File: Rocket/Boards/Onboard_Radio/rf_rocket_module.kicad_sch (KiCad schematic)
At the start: 12 parts

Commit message: schematic ready for review
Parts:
- R17, R18, R19: MPN (none) -> CRCW06030000Z0EA; Manufacturer (none) -> Vishay Dale
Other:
- sheet CAN_Termination ports: added none; removed CAN2_RX, CAN2_TX, CAN_STB2
- sheet MCU ports: added none; removed CAN2_RX, CAN2_TX, CAN_STB2
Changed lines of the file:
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@@
+	(wire
+		(pts
+			(xy 53.34 105.41) (xy 77.47 105.41)
+		)
+		(stroke
+			(width 0)
+			(type default)
+		)
+	)
 	(wire
 		(pts
@@
 	(wire
 		(pts
-			(xy 53.34 87.63) (xy 77.47 87.63)
-		)
-		(stroke
-			(width 0)
-			(type default)
-		)
-	)
-	(wire
-		(pts
 			(xy 124.46 22.86) (xy 157.48 22.86)
 		)
@@
 	(wire
 		(pts
-			(xy 53.34 97.79) (xy 77.47 97.79)
-		)
-		(stroke
-			(width 0)
-			(type default)
-		)
-	)
-	(wire
-		(pts
 			(xy 43.18 166.37) (xy 49.53 166.37)
 		)
@@
 	(wire
 		(pts
-			(xy 53.34 90.17) (xy 77.47 90.17)
-		)
-		(stroke
-			(width 0)
-			(type default)
-		)
-	)
-	(wire
-		(pts
 			(xy 54.61 22.86) (xy 52.07 22.86)
 		)
@@
 		(pts
 			(xy 43.18 173.99) (xy 49.53 173.99)
-		)
-		(stroke
-			(width 0)
-			(type default)
-		)
-	)
-	(wire
-		(pts
-			(xy 53.34 105.41) (xy 77.47 105.41)
 		)
 		(stroke
@@
 			)
 		)
-		(property "Datasheet" ""
+		(property "Datasheet" "https://www.vishay.com/docs/20035/dcrcwe3.pdf"
 			(at 58.42 33.02 0)
 			(hide yes)
@@
 			)
 		)
-		(property "Description" "Resistor"
+		(property "Description" "0 Ohms Jumper 0.125W, 1/8W Chip Resistor 0603 (1608 Metric) Automotive AEC-Q200 Thick Film"
 			(at 58.42 33.02 0)
 			(hide yes)
@@
 		)
 		(property "KLC_S4.1" ""
+			(at 58.42 33.02 90)
+			(hide yes)
+			(show_name no)
+			(do_not_autoplace no)
+			(effects
+				(font
+					(size 1.27 1.27)
+				)
+			)
+		)
+		(property "MPN" "CRCW06030000Z0EA"
+			(at 58.42 33.02 90)
+			(hide yes)
+			(show_name no)
+			(do_not_autoplace no)
+			(effects
+				(font
+					(size 1.27 1.27)
+				)
+			)
+		)
+		(property "Manufacturer" "Vishay Dale"
 			(at 58.42 33.02 90)
 			(hide yes)
@@
 			)
 		)
-		(property "Datasheet" ""
+		(property "Datasheet" "https://www.vishay.com/docs/20035/dcrcwe3.pdf"
 			(at 58.42 27.94 0)
 			(hide yes)
@@
 			)
 		)
-		(property "Description" "Resistor"
+		(property "Description" "0 Ohms Jumper 0.125W, 1/8W Chip Resistor 0603 (1608 Metric) Automotive AEC-Q200 Thick Film"
 			(at 58.42 27.94 0)
 			(hide yes)
@@
 		)
 		(property "KLC_S4.1" ""
+			(at 58.42 27.94 90)
+			(hide yes)
+			(show_name no)
+			(do_not_autoplace no)
+			(effects
+				(font
+					(size 1.27 1.27)
+				)
+			)
+		)
+		(property "MPN" "CRCW06030000Z0EA"
+			(at 58.42 27.94 90)
+			(hide yes)
+			(show_name no)
+			(do_not_autoplace no)
+			(effects
+				(font
+					(size 1.27 1.27)
+				)
+			)
+		)
+		(property "Manufacturer" "Vishay Dale"
 			(at 58.42 27.94 90)
 			(hide yes)
@@
 			)
 		)
-		(property "Datasheet" ""
+		(property "Datasheet" "https://www.vishay.com/docs/20035/dcrcwe3.pdf"
 			(at 58.42 22.86 0)
 			(hide yes)
@@
 			)
 		)
-		(property "Description" "Resistor"
+		(property "Description" "0 Ohms Jumper 0.125W, 1/8W Chip Resistor 0603 (1608 Metric) Automotive AEC-Q200 Thick Film"
 			(at 58.42 22.86 0)
 			(hide yes)
@@
 		)
 		(property "KLC_S4.1" ""
+			(at 58.42 22.86 90)
+			(hide yes)
+			(show_name no)
+			(do_not_autoplace no)
+			(effects
+				(font
+					(size 1.27 1.27)
+				)
+			)
+		)
+		(property "MPN" "CRCW06030000Z0EA"
+			(at 58.42 22.86 90)
+			(hide yes)
+			(show_name no)
+			(do_not_autoplace no)
+			(effects
+				(font
+					(size 1.27 1.27)
+				)
+			)
+		)
+		(property "Manufacturer" "Vishay Dale"
 			(at 58.42 22.86 90)
 			(hide yes)
@@
 			)
 		)
+		(pin "CAN1_RX" input
+			(at 77.47 80.01 180)
+			(effects
+				(font
+					(size 1.27 1.27)
+				)
+				(justify left)
+			)
+		)
+		(pin "CAN1_TX" input
+			(at 77.47 82.55 180)
+			(effects
+				(font
+					(size 1.27 1.27)
+				)
+				(justify left)
+			)
+		)
+		(pin "CAN_STB1" input
+			(at 77.47 95.25 180)
+			(effects
+				(font
+					(size 1.27 1.27)
+				)
+				(justify left)
+			)
+		)
 		(pin "CAN2_AUX" input
 			(at 77.47 105.41 180)
-			(effects
-				(font
-					(size 1.27 1.27)
-				)
-				(justify left)
-			)
-		)
-		(pin "CAN1_RX" input
-			(at 77.47 80.01 180)
-			(effects
-				(font
-					(size 1.27 1.27)
-				)
-				(justify left)
-			)
-		)
-		(pin "CAN1_TX" input
-			(at 77.47 82.55 180)
-			(effects
-				(font
-					(size 1.27 1.27)
-				)
-				(justify left)
-			)
-		)
-		(pin "CAN2_RX" input
-			(at 77.47 87.63 180)
-			(effects
-				(font
-					(size 1.27 1.27)
-				)
-				(justify left)
-			)
-		)
-		(pin "CAN2_TX" input
-			(at 77.47 90.17 180)
-			(effects
-				(font
-					(size 1.27 1.27)
-				)
-				(justify left)
-			)
-		)
-		(pin "CAN_STB1" input
-			(at 77.47 95.25 180)
-			(effects
-				(font
-					(size 1.27 1.27)
-				)
-				(justify left)
-			)
-		)
-		(pin "CAN_STB2" input
-			(at 77.47 97.79 180)
 			(effects
 				(font
@@
 			)
 		)
+		(pin "CAN_PWR_IN" input
+			(at 53.34 74.93 0)
+			(effects
+				(font
+					(size 1.27 1.27)
+				)
+				(justify right)
+			)
+		)
+		(pin "CAN_STB1" input
+			(at 53.34 95.25 0)
+			(effects
+				(font
+					(size 1.27 1.27)
+				)
+				(justify right)
+			)
+		)
 		(pin "CAN2_AUX" input
 			(at 53.34 105.41 0)
 			(effects
 				(font
-					(size 1.27 1.27)
-				)
-				(justify right)
-			)
-		)
-		(pin "CAN_PWR_IN" input
-			(at 53.34 74.93 0)
-			(effects
-				(font
-					(size 1.27 1.27)
-				)
-				(justify right)
-			)
-		)
-		(pin "CAN2_RX" input
-			(at 53.34 90.17 0)
-			(effects
-				(font
-					(size 1.27 1.27)
-				)
-				(justify right)
-			)
-		)
-		(pin "CAN2_TX" input
-			(at 53.34 87.63 0)
-			(effects
-				(font
-					(size 1.27 1.27)
-				)
-				(justify right)
-			)
-		)
-		(pin "CAN_STB1" input
-			(at 53.34 95.25 0)
-			(effects
-				(font
-					(size 1.27 1.27)
-				)
-				(justify right)
-			)
-		)
-		(pin "CAN_STB2" input
-			(at 53.34 97.79 0)
-			(effects
-				(font

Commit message: updates
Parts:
- removed R17, R18, R19: 0R, Resistor_SMD:R_0603_1608Metric, symbol Device:R
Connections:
- net Power Input/+7V4 renamed Power Input/+7V4_Input
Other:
- sheet Power Input ports: added +3V3A_Input, +3V3_Input, +5V_Input, +7V4_Input; removed +3V3, +3V3A, +5V, +7V4
- moved on the sheet: R20

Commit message: everything minus trace impedance and via stictching
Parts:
- H1, H2, H3, H4: footprint MountingHole:MountingHole_3.2mm_M3 -> MountingHole:MountingHole_3.2mm_M3_DIN965_Pad
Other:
- sheet MCU ports: added 3V3A_LDO_EN, 3V3_LDO_EN; removed none
- sheet Power Input ports: added 3V3A_LDO_EN, 3V3_LDO_EN; removed none
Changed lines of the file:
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@@
+	(wire
+		(pts
+			(xy 52.07 46.99) (xy 77.47 46.99)
+		)
+		(stroke
+			(width 0)
+			(type default)
+		)
+	)
 	(wire
 		(pts
@@
 		(pts
 			(xy 153.67 44.45) (xy 157.48 44.45)
+		)
+		(stroke
+			(width 0)
+			(type default)
+		)
+	)
+	(wire
+		(pts
+			(xy 52.07 49.53) (xy 77.47 49.53)
 		)
 		(stroke
@@
 			)
 		)
-		(property "Footprint" "MountingHole:MountingHole_3.2mm_M3"
+		(property "Footprint" "MountingHole:MountingHole_3.2mm_M3_DIN965_Pad"
 			(at 40.64 166.37 0)
 			(hide yes)
@@
 			)
 		)
-		(property "Footprint" "MountingHole:MountingHole_3.2mm_M3"
+		(property "Footprint" "MountingHole:MountingHole_3.2mm_M3_DIN965_Pad"
 			(at 40.64 151.13 0)
 			(hide yes)
@@
 			)
 		)
-		(property "Footprint" "MountingHole:MountingHole_3.2mm_M3"
+		(property "Footprint" "MountingHole:MountingHole_3.2mm_M3_DIN965_Pad"
 			(at 40.64 173.99 0)
 			(hide yes)
@@
 			)
 		)
-		(property "Footprint" "MountingHole:MountingHole_3.2mm_M3"
+		(property "Footprint" "MountingHole:MountingHole_3.2mm_M3_DIN965_Pad"
 			(at 40.64 158.75 0)
 			(hide yes)
@@
 			)
 		)
+		(pin "3V3A_LDO_EN" input
+			(at 52.07 46.99 0)
+			(effects
+				(font
+					(size 1.27 1.27)
+				)
+				(justify right)
+			)
+		)
+		(pin "3V3_LDO_EN" input
+			(at 52.07 49.53 0)
+			(effects
+				(font
+					(size 1.27 1.27)
+				)
+				(justify right)
+			)
+		)
 		(instances
 			(project "rf_rocket_module"
@@
 			(effects
 				(font
+					(size 1.27 1.27)
+				)
+				(justify left)
+			)
+		)
+		(pin "3V3A_LDO_EN" input
+			(at 77.47 46.99 180)
+			(effects
+				(font
+					(size 1.27 1.27)
+				)
+				(justify left)
+			)
+		)
+		(pin "3V3_LDO_EN" input
+			(at 77.47 49.53 180)
+			(effects
+				(font

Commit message: needs pcb and schematic review
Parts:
- R20: LCSC Part # (none) -> C844915
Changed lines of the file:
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@@
+			)
+		)
+		(property "LCSC Part #" "C844915"
+			(at 58.42 38.1 90)
+			(hide yes)
+			(show_name no)
+			(do_not_autoplace no)
+			(effects
+				(font
+					(size 1.27 1.27)
+				)
 			)
 		)

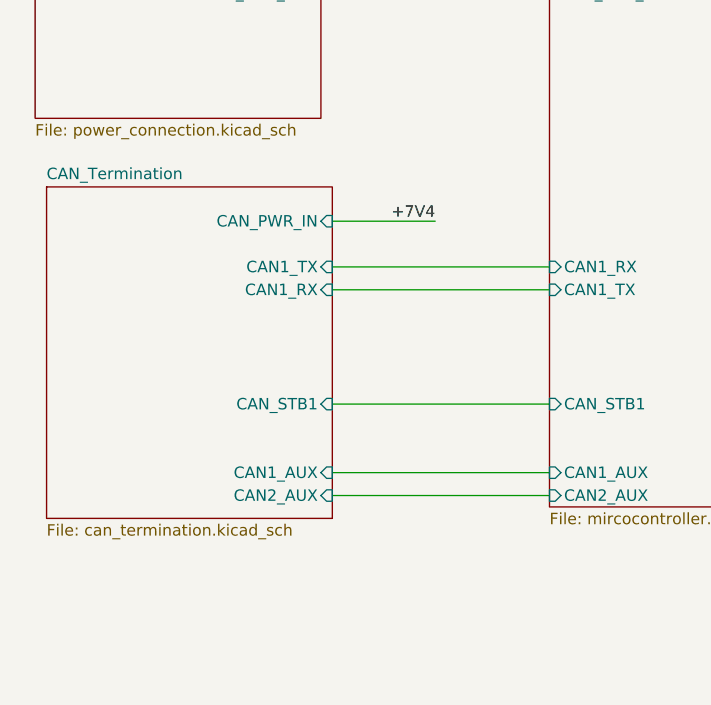
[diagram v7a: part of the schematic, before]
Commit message: updated swd and crystal
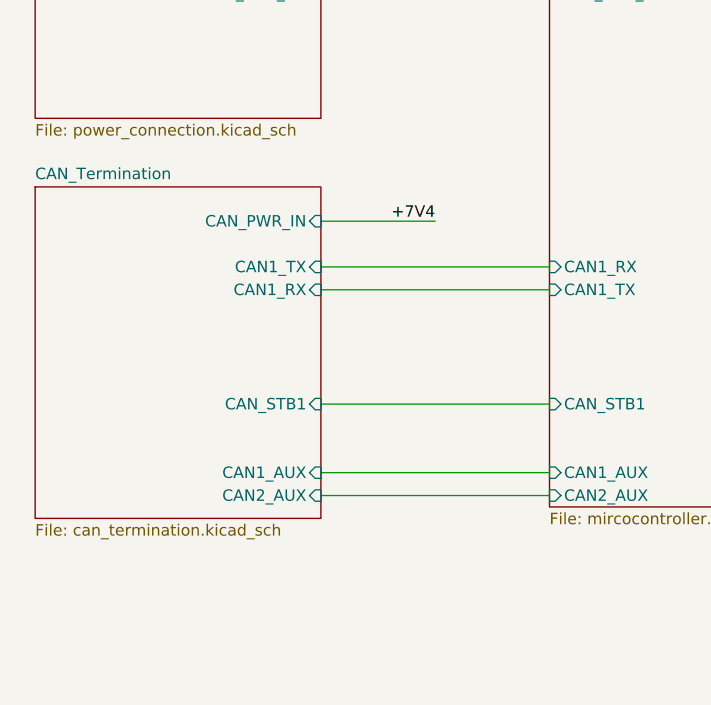
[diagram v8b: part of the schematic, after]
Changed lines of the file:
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@@
 	(wire
 		(pts
-			(xy 53.34 105.41) (xy 77.47 105.41)
+			(xy 52.07 105.41) (xy 77.47 105.41)
 		)
 		(stroke
@@
 	(wire
 		(pts
-			(xy 64.77 74.93) (xy 53.34 74.93)
+			(xy 64.77 74.93) (xy 52.07 74.93)
 		)
 		(stroke
@@
 	(wire
 		(pts
-			(xy 53.34 95.25) (xy 77.47 95.25)
-		)
-		(stroke
-			(width 0)
-			(type default)
-		)
-	)
-	(wire
-		(pts
-			(xy 53.34 80.01) (xy 77.47 80.01)
+			(xy 52.07 95.25) (xy 77.47 95.25)
+		)
+		(stroke
+			(width 0)
+			(type default)
+		)
+	)
+	(wire
+		(pts
+			(xy 52.07 80.01) (xy 77.47 80.01)
 		)
 		(stroke
@@
 	(wire
 		(pts
-			(xy 53.34 102.87) (xy 77.47 102.87)
+			(xy 52.07 102.87) (xy 77.47 102.87)
 		)
 		(stroke
@@
 	(wire
 		(pts
-			(xy 53.34 82.55) (xy 77.47 82.55)
+			(xy 52.07 82.55) (xy 77.47 82.55)
 		)
 		(stroke
@@
 	)
 	(sheet
-		(at 21.59 71.12)
+		(at 20.32 71.12)
 		(size 31.75 36.83)
 		(exclude_from_sim no)
@@
 		)
 		(property "Sheetname" "CAN_Termination"
-			(at 21.59 70.4084 0)
+			(at 20.32 70.4084 0)
 			(show_name no)
 			(do_not_autoplace no)
@@
 		)
 		(property "Sheetfile" "can_termination.kicad_sch"
-			(at 21.59 108.5346 0)
+			(at 20.32 108.5346 0)
 			(show_name no)
 			(do_not_autoplace no)
@@
 		)
 		(pin "CAN1_RX" input
-			(at 53.34 82.55 0)
+			(at 52.07 82.55 0)
 			(effects
 				(font
@@
 		)
 		(pin "CAN1_TX" input
-			(at 53.34 80.01 0)
+			(at 52.07 80.01 0)
 			(effects
 				(font
@@
 		)
 		(pin "CAN1_AUX" input
-			(at 53.34 102.87 0)
+			(at 52.07 102.87 0)
 			(effects
 				(font
@@
 		)
 		(pin "CAN_PWR_IN" input
-			(at 53.34 74.93 0)
+			(at 52.07 74.93 0)
 			(effects
 				(font
@@
 		)
 		(pin "CAN_STB1" input
-			(at 53.34 95.25 0)
+			(at 52.07 95.25 0)
 			(effects
 				(font
@@
 		)
 		(pin "CAN2_AUX" input
-			(at 53.34 105.41 0)
-			(effects
-				(font
+			(at 52.07 105.41 0)
+			(effects
+				(font
